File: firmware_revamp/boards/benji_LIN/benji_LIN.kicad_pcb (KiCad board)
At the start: 2 copper layers, 42.9 x 68.3 mm, 37 parts, among them J1 CONN_02X03, J2 Conn_01x09, J3 Conn_01x09, J4 CONN_01X03, J5 CONN_01x02, J6 CONN_01X03, J7 CONN_01x02, U1 MCP2561-E_SN, U2 ATMEGA16M1, U3 TLIN1021DRQ1, Y1 Crystal_SMD

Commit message: Fixed some silkscreens, and used smaller length headers
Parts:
- added G***: LOGO, footprints:phoenix, B.Cu at (324.9, 96.3)

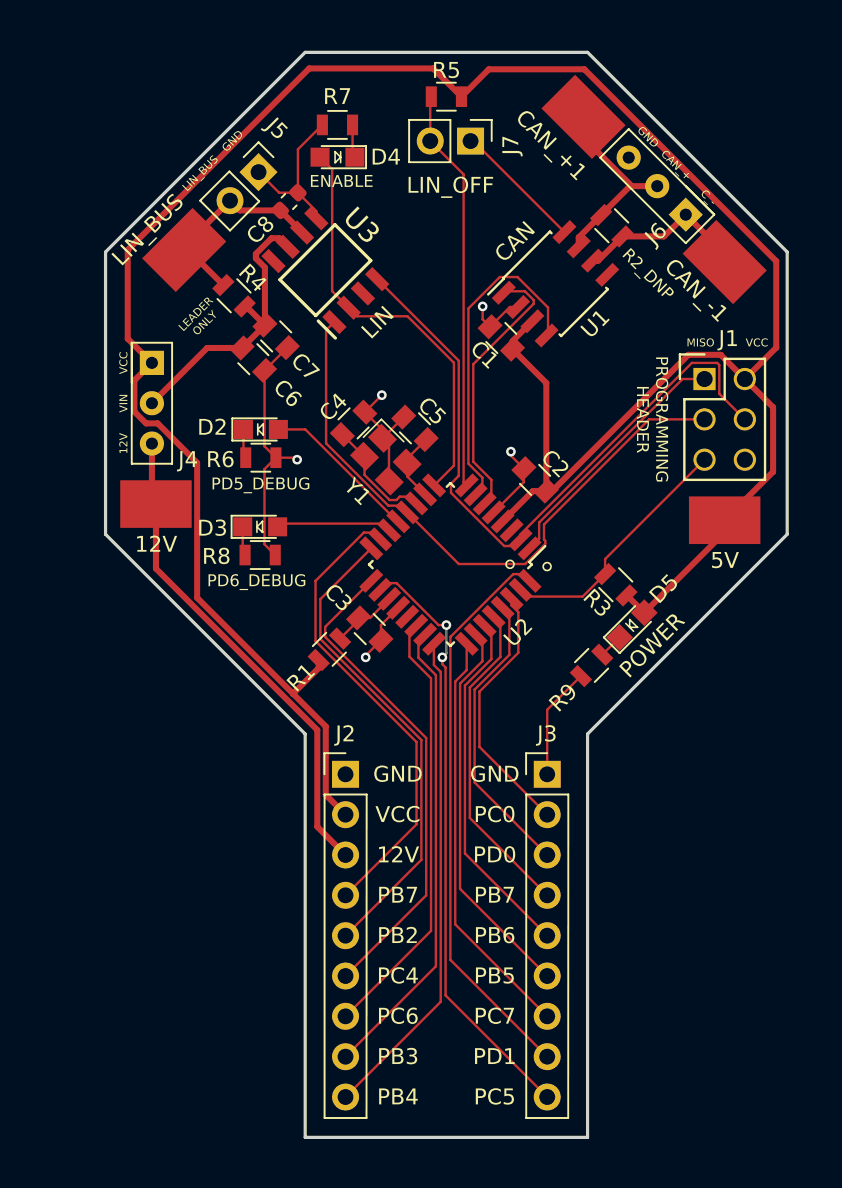
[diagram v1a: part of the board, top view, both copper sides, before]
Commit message: Added 12V Led and Silks
Added Olin Logo and whitespace for notes
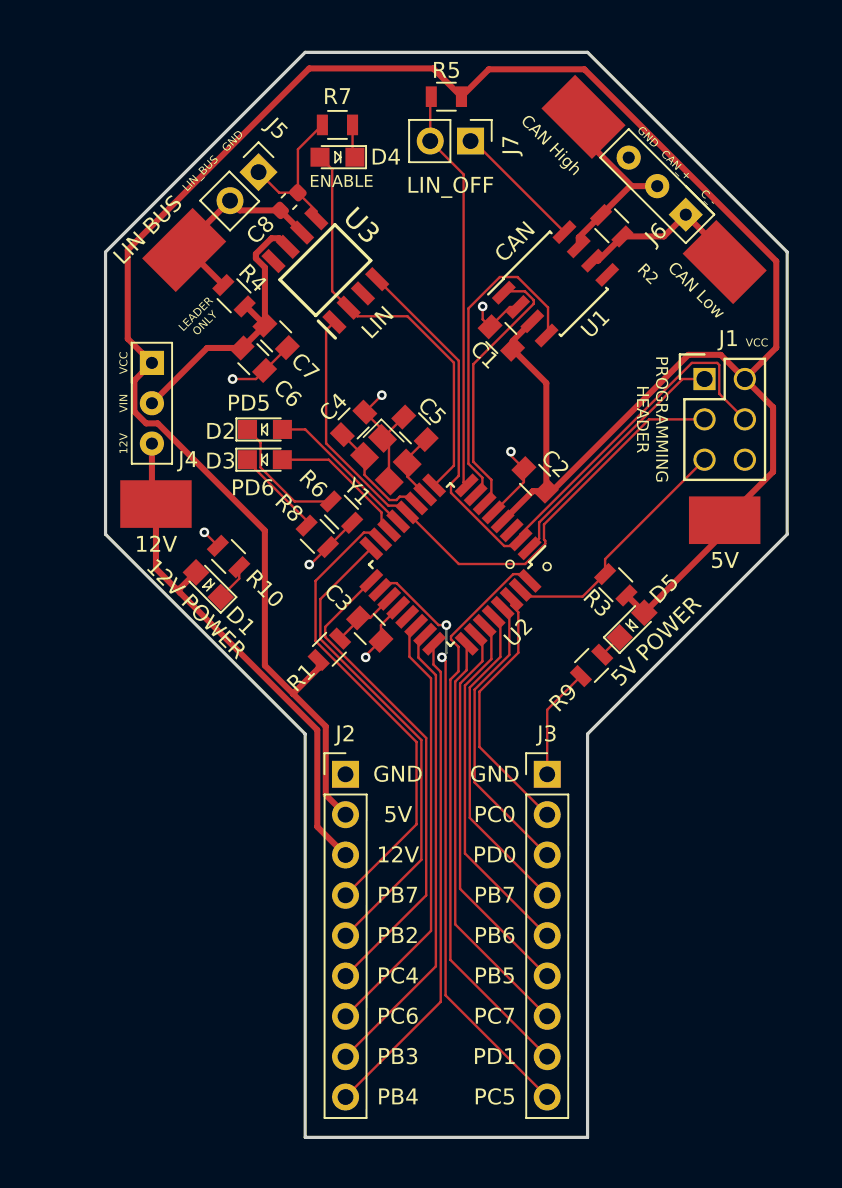
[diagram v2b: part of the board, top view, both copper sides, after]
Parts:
- removed the G*** at (324.9, 96.3)
- added D1: LED_0805_Amber, footprints:LED_0805_OEM, F.Cu at (93.2, 88.4)
- added G***: LOGO, footprints:Olin_Electric_Smaller, B.Cu at (108.0, 72.9)
- added R10: R_2.2K, footprints:R_0805_OEM, F.Cu at (94.5, 86.6)
- CAN High: renamed from CAN_+1
- CAN Low: renamed from CAN_-1
- LIN BUS: renamed from LIN_BUS
- moved R6 6.13 mm to (101.6, 83.8), turned to 315 degrees
- moved D3 4.24 mm to (96.8, 80.5)
- moved R8 3.79 mm to (100.1, 85.3), turned to 315 degrees
- moved D2 0.25 mm to (96.8, 78.6)
- renumbered R2_DNP to R2
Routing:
- net GND: track 62.3 -> 55.7 mm, vias 5 -> 7
- net Net-(D2-Pad1): track 1.84 -> 8.05 mm
- net Net-(D3-Pad1): track 1.84 -> 5.70 mm
- net Net-(D1-Pad1): track 0.00 -> 2.37 mm
- net /12V: track 31.0 -> 32.6 mm
- net /RIGHT_DEBUG: track 7.29 -> 8.95 mm
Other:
- board text added: "12V POWER"
- board text added: "5V"
- board text added: "5V POWER"
- board text added: "Main Node:"
- board text added: "PD5"
- board text added: "PD6"
- board text removed: "MISO"
- board text removed: "PD5_DEBUG"
- board text removed: "PD6_DEBUG"
- board text removed: "POWER"
